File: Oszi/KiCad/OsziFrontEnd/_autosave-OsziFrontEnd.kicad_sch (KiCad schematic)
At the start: 0 parts

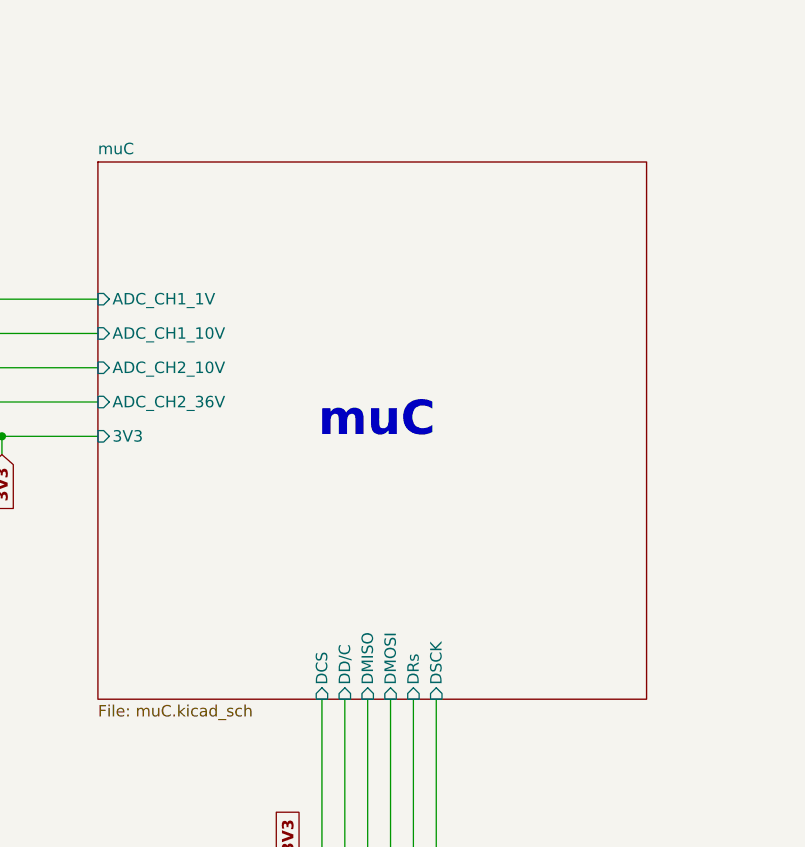
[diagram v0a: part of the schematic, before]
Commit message: added buttons 4 display
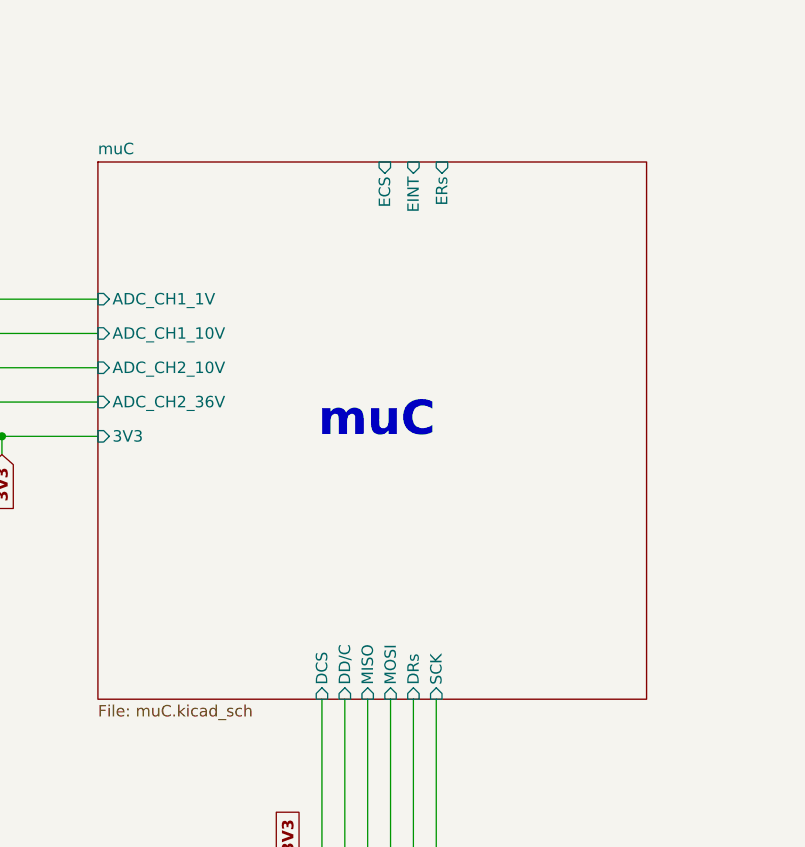
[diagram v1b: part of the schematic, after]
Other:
- sheet muC ports: added ECS, EINT, ERs, MISO, MOSI, SCK; removed DMISO, DMOSI, DSCK
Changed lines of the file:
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@@
-			)
-		)
-		(pin "DMISO" input
-			(at 294.64 161.798 270)
-			(effects
-				(font
-					(size 1.27 1.27)
-				)
-				(justify left)
-			)
-		)
-		(pin "DMOSI" input
-			(at 297.18 161.798 270)
-			(effects
-				(font
-					(size 1.27 1.27)
-				)
-				(justify left)
 			)
 		)
@@
 			)
 		)
-		(pin "DSCK" input
+		(pin "ECS" input
+			(at 296.545 102.108 90)
+			(effects
+				(font
+					(size 1.27 1.27)
+				)
+				(justify right)
+			)
+		)
+		(pin "EINT" input
+			(at 299.72 102.108 90)
+			(effects
+				(font
+					(size 1.27 1.27)
+				)
+				(justify right)
+			)
+		)
+		(pin "ERs" input
+			(at 302.895 102.108 90)
+			(effects
+				(font
+					(size 1.27 1.27)
+				)
+				(justify right)
+			)
+		)
+		(pin "MISO" input
+			(at 294.64 161.798 270)
+			(effects
+				(font
+					(size 1.27 1.27)
+				)
+				(justify left)
+			)
+		)
+		(pin "MOSI" input
+			(at 297.18 161.798 270)
+			(effects
+				(font
+					(size 1.27 1.27)
+				)
+				(justify left)
+			)
+		)
+		(pin "SCK" input
 			(at 302.26 161.798 270)
 			(effects
